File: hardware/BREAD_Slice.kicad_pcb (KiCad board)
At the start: 2 copper layers, 72.6 x 100 mm, 16 parts, among them J1 Conn_01x10_Female, J2 I2C_01x04

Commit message: Initial commit
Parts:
- removed C4: 22uF, Capacitor_SMD:C_1206_3216Metric
- removed D1: WS2812B_5050, SparkFun-LED:WS2812-5050-4PIN
- removed HS1: Heatsink_Pad, SparkFun-Fuse:Thermal Pad
- removed L1: 4.7uH, Inductor_SMD:L_1210_3225Metric
- added FB1: Ferrite_Bead_Small, OCI_UPL_FOOTPRINTS:R_1206_HandSoldering, B.Cu at (175.9, 81.4)
- added FB2: Ferrite_Bead_Small, OCI_UPL_FOOTPRINTS:R_1206_HandSoldering, B.Cu at (175.9, 76.3)
- added J3: Screw_Terminal_01x02, OCI_UPL_FOOTPRINTS:TerminalBlock_Pheonix_MKDS1.5-2pol, F.Cu at (184.8, 62.3)
- added J4: Screw_Terminal_01x02, OCI_UPL_FOOTPRINTS:TerminalBlock_Pheonix_MKDS1.5-2pol, F.Cu at (184.8, 100.4)
- added Q1: TIP120, Package_TO_SOT_THT:TO-220-3_Vertical, F.Cu at (144.2, 85.2)
- added Q2: TIP120, Package_TO_SOT_THT:TO-220-3_Vertical, F.Cu at (144.2, 72.5)
- added R1: 10k, OCI_UPL_FOOTPRINTS:R_1206_HandSoldering, B.Cu at (174.7, 100.4)
- added R2: 10k, OCI_UPL_FOOTPRINTS:R_1206_HandSoldering, B.Cu at (159.4, 91.5)
- added R3: 10k, OCI_UPL_FOOTPRINTS:R_1206_HandSoldering, B.Cu at (159.4, 83.9)
- C1: value 22uF -> 10uF_t; footprint Capacitor_SMD:C_1206_3216Metric -> OCI_UPL_FOOTPRINTS:C_2312
- C2: value 100nF -> 10uF_t; footprint Capacitor_SMD:C_1206_3216Metric -> OCI_UPL_FOOTPRINTS:C_2312
- C3: value 22uF -> 0.01 uF; footprint Capacitor_SMD:C_1206_3216Metric -> OCI_UPL_FOOTPRINTS:C_1206_HandSoldering
- H1, H4: footprint MountingHole:MountingHole_5mm -> MountingHole:MountingHole_3.2mm_M3_DIN965_Pad
- H2: renamed from H3; footprint MountingHole:MountingHole_5mm -> MountingHole:MountingHole_3.2mm_M3_DIN965_Pad
- H3: renamed from H2; footprint MountingHole:MountingHole_5mm -> MountingHole:MountingHole_3.2mm_M3_DIN965_Pad
- J2: value I2C_01x04 -> Screw_Terminal_01x02; footprint Connector_JST:JST_SH_SM04B-SRSS-TB_1x04-1MP_P1.00mm_Horizontal -> OCI_UPL_FOOTPRINTS:TerminalBlock_Pheonix_MKDS1.5-2pol; moved to F.Cu
- U1: value ~ -> MAX31855KASA; footprint Package_TO_SOT_SMD:TSOT-23-6 -> Package_SO:SOIC-8_3.9x4.9mm_P1.27mm
- moved Logo1 75.1 mm to (166.6, 135.8), turned to 0 degrees
- moved J2 69.4 mm to (184.8, 76.3), turned to -90 degrees
- moved C3 54.1 mm to (169.6, 78.8), turned to 90 degrees
- moved U1 53.6 mm to (159.4, 78.8), turned to 180 degrees
- moved C1 35.5 mm to (157.6, 99.0), turned to 0 degrees
- moved C2 32.3 mm to (157.6, 107.8), turned to 0 degrees
- moved A1 7.59 mm to (135.0, 100.0)
- moved J1 3.43 mm to (129.6, 78.8)
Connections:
- A1 pad 1: unconnected-(A1-D1/TX-Pad1) -> Net-(A1-Pad1)
- A1 pad 10: unconnected-(A1-D7-Pad10) -> Net-(A1-Pad10)
- A1 pad 11: unconnected-(A1-D8-Pad11) -> Net-(A1-Pad11)
- A1 pad 12: unconnected-(A1-D9-Pad12) -> /SS
- A1 pad 13: unconnected-(A1-D10-Pad13) -> /DATA
- A1 pad 14: unconnected-(A1-D11-Pad14) -> /CLK
- A1 pad 15: unconnected-(A1-D12-Pad15) -> Net-(A1-Pad15)
- A1 pad 16: unconnected-(A1-D13-Pad16) -> Net-(A1-Pad16)
- A1 pad 17: unconnected-(A1-3V3-Pad17) -> Net-(A1-Pad17)
- A1 pad 18: unconnected-(A1-AREF-Pad18) -> Net-(A1-Pad18)
- A1 pad 19: unconnected-(A1-A0-Pad19) -> /TMSTR
- A1 pad 2: unconnected-(A1-D0/RX-Pad2) -> Net-(A1-Pad2)
- A1 pad 20: unconnected-(A1-A1-Pad20) -> Net-(A1-Pad20)
- A1 pad 21: unconnected-(A1-A2-Pad21) -> Net-(A1-Pad21)
- A1 pad 22: unconnected-(A1-A3-Pad22) -> Net-(A1-Pad22)
- A1 pad 25: unconnected-(A1-A6-Pad25) -> Net-(A1-Pad25)
- A1 pad 26: unconnected-(A1-A7-Pad26) -> Net-(A1-Pad26)
- A1 pad 28: unconnected-(A1-~{RESET}-Pad28) -> Net-(A1-Pad28)
- A1 pad 3: unconnected-(A1-~{RESET}-Pad3) -> Net-(A1-Pad3)
- A1 pad 30: unconnected-(A1-VIN-Pad30) -> +12V
- A1 pad 8: /LED -> Net-(A1-Pad8)
- A1 pad 9: unconnected-(A1-D6-Pad9) -> /PWM
- C1 pad 1: GND -> +12V
- C1 pad 2: +12V -> GND
- C2 pad 1: Net-(U1-SW) -> +5V
- C2 pad 2: Net-(U1-BST) -> GND
- C3 pad 1: GND -> Net-(C3-Pad1)
- C3 pad 2: +5V -> Net-(C3-Pad2)
- J2 pad 1: GND -> Net-(FB2-Pad2)
- J2 pad 2: +5V -> Net-(FB1-Pad2)
- U1 pad 1: +5V -> GND
- U1 pad 2: +12V -> Net-(C3-Pad2)
- U1 pad 3: +12V -> Net-(C3-Pad1)
- U1 pad 4: GND -> +5V
- U1 pad 5: Net-(U1-SW) -> /CLK
- U1 pad 6: Net-(U1-BST) -> /SS
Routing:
- net /SS: track 0.00 -> 96.8 mm, vias 0 -> 2
- net GND: track 19.6 -> 91.1 mm, vias 14 -> 2
- net /DATA: track 0.00 -> 69.2 mm
- net /CLK: track 0.00 -> 68.8 mm
- net Net-(J3-Pad1): track 0.00 -> 65.2 mm
- net Net-(J3-Pad2): track 0.00 -> 63.8 mm
- net /E_STOP: track 30.1 -> 93.2 mm, vias 0 -> 2
- net +5V: track 108.9 -> 51.7 mm, vias 1 -> 0
- net /LED: track 51.5 -> 0.00 mm
- net /TMSTR: track 0.00 -> 46.6 mm
- net /PWM: track 0.00 -> 41.9 mm
- net /I2C_CLK: track 78.5 -> 42.6 mm
- net /I2C_DAT: track 76.6 -> 41.8 mm
- net +12V: track 46.8 -> 81.6 mm, vias 0 -> 2
- net Net-(C3-Pad2): track 0.00 -> 13.4 mm
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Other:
- board size 72.6 x 100 mm -> 70 x 100 mm
- board text added: "+"
- board text added: "-"
- board text added: "Heater"
- board text added: "Heating Slice SLC_HEAT R0 2021"
- board text added: "Thermistor Input"
- board text added: "Thermocouple Input"
- board text removed: "12V"
- board text removed: "12V->5V Reg"
- board text removed: "5V I2C Connector"
- board text removed: "ARDUINO NANO"
- board text removed: "BREAD Slice Template SLC_TEMP <version> <year>"
- board text removed: "ESTOP"
- board text removed: "GND"
- board text removed: "INT"
- board text removed: "LED"
- board text removed: "SCL"
- board text removed: "SDA"
- board text removed: "SYNC"

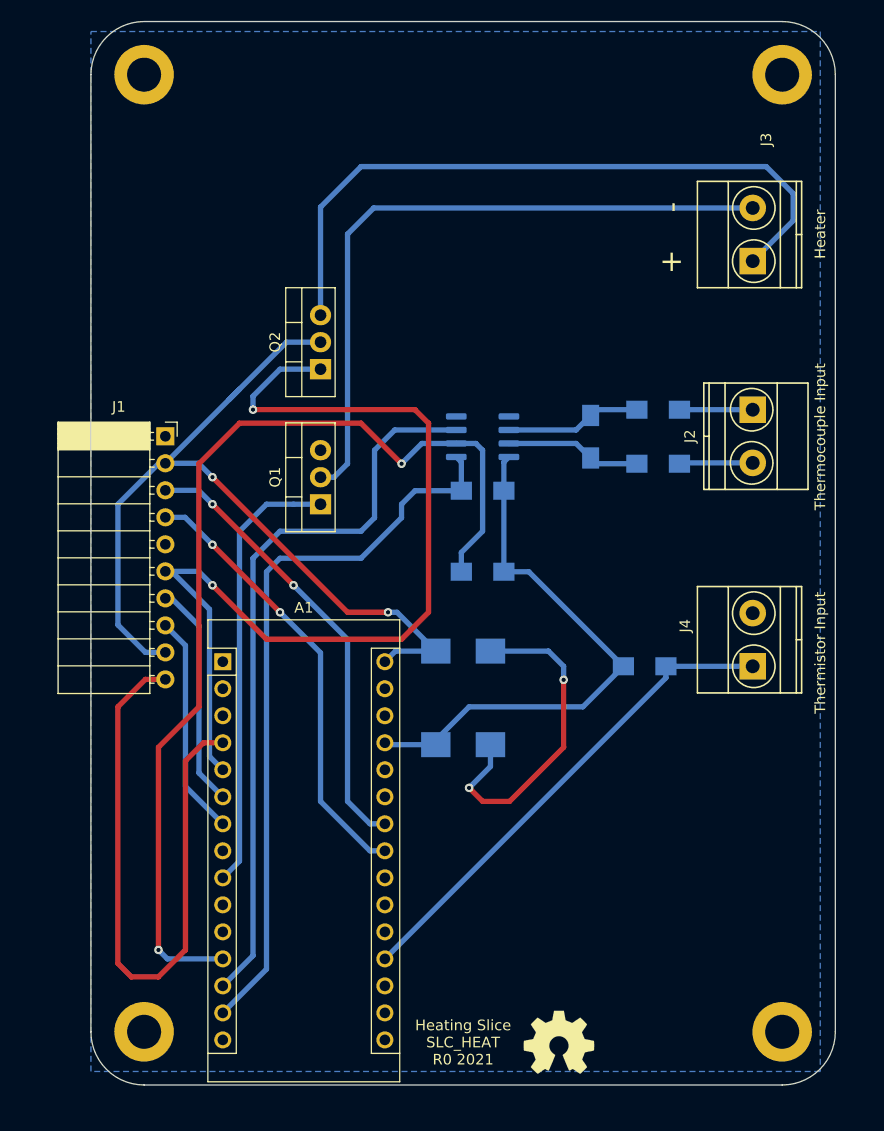
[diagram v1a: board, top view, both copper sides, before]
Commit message: upgraded by duplicating ciruit, new core, all back copper
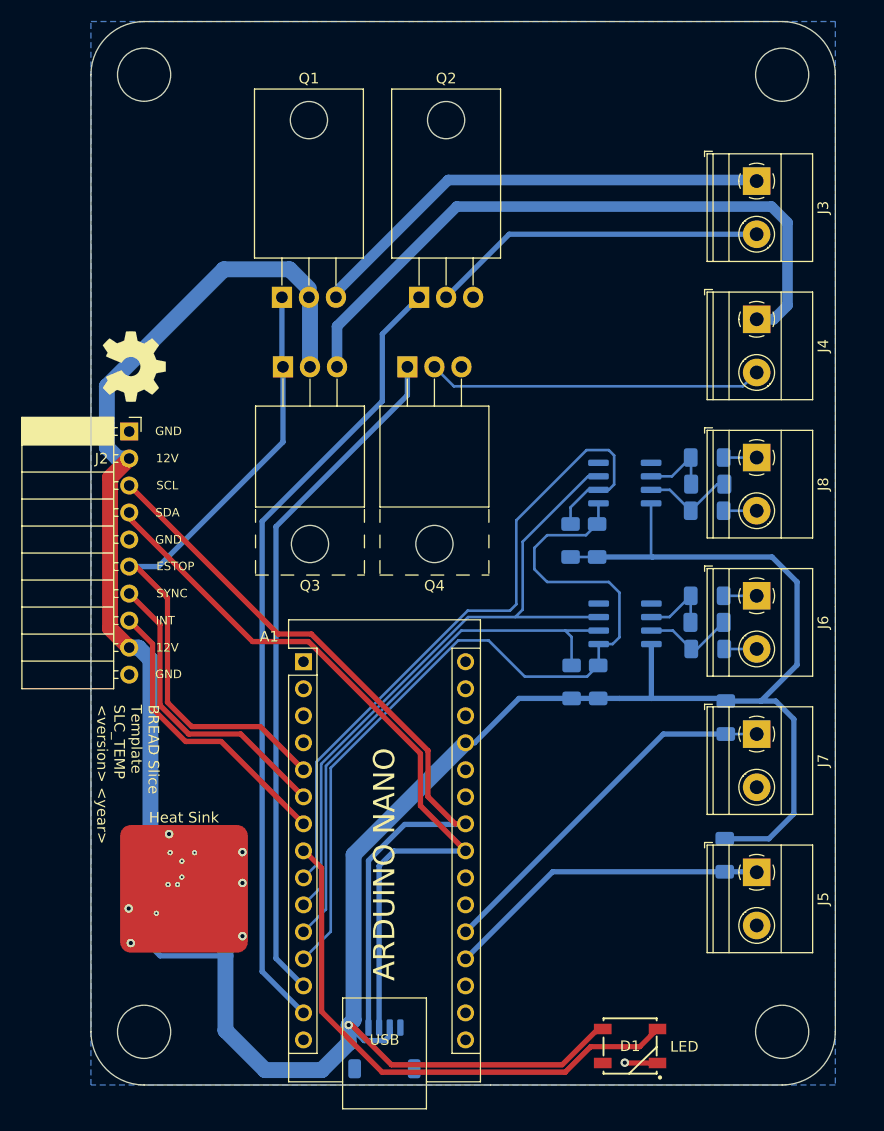
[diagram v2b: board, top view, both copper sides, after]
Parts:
- removed the J2 at (184.8, 76.3)
- added C4: 22uF, Capacitor_SMD:C_1206_3216Metric, B.Cu at (133.8, 116.5)
- added C5: 0.01 uF, Capacitor_SMD:C_1206_3216Metric_Pad1.33x1.80mm_HandSolder, B.Cu at (180.5, 96.3)
- added C6: 0.01 uF, Capacitor_SMD:C_1206_3216Metric_Pad1.33x1.80mm_HandSolder, B.Cu at (180.6, 83.3)
- added D1: WS2812B_5050, SparkFun-LED:WS2812-5050-4PIN, F.Cu at (173.3, 136.1)
- added FB3: Ferrite_Bead_Small, Resistor_SMD:R_1206_3216Metric_Pad1.30x1.75mm_HandSolder, B.Cu at (180.6, 85.8)
- added FB4: Ferrite_Bead_Small, Resistor_SMD:R_1206_3216Metric_Pad1.30x1.75mm_HandSolder, B.Cu at (180.6, 80.8)
- added HS1: Heatsink_Pad, KML-Custom:Thermal Pad, F.Cu at (131.3, 121.4)
- added J1: I2C_01x04, Connector_JST:JST_SH_SM04B-SRSS-TB_1x04-1MP_P1.00mm_Horizontal, B.Cu at (150.2, 136.4)
- added J5: Screw_Terminal_01x02, TerminalBlock_Phoenix:TerminalBlock_Phoenix_MKDS-1,5-2_1x02_P5.00mm_Horizontal, F.Cu at (185.2, 119.8)
- added J6: Screw_Terminal_01x02, TerminalBlock_Phoenix:TerminalBlock_Phoenix_MKDS-1,5-2_1x02_P5.00mm_Horizontal, F.Cu at (185.2, 93.8)
- added J7: Screw_Terminal_01x02, TerminalBlock_Phoenix:TerminalBlock_Phoenix_MKDS-1,5-2_1x02_P5.00mm_Horizontal, F.Cu at (185.2, 106.8)
- added J8: Screw_Terminal_01x02, TerminalBlock_Phoenix:TerminalBlock_Phoenix_MKDS-1,5-2_1x02_P5.00mm_Horizontal, F.Cu at (185.2, 80.8)
- added L1: 4.7uH, Inductor_SMD:L_1210_3225Metric, B.Cu at (133.8, 122.8)
- added Q3: TIP120, Package_TO_SOT_THT:TO-220-3_Horizontal_TabUp, F.Cu at (140.7, 72.3)
- added Q4: TIP120, Package_TO_SOT_THT:TO-220-3_Horizontal_TabUp, F.Cu at (152.4, 72.3)
- added R4: 10k, Resistor_SMD:R_1206_3216Metric_Pad1.30x1.75mm_HandSolder, B.Cu at (170.2, 88.6)
- added R5: 10k, Resistor_SMD:R_1206_3216Metric_Pad1.30x1.75mm_HandSolder, B.Cu at (167.7, 88.6)
- added R6: 10k, Resistor_SMD:R_1206_3216Metric_Pad1.30x1.75mm_HandSolder, B.Cu at (182.3, 105.2)
- added U2: MAX31855KASA, Package_SO:SOIC-8_3.9x4.9mm_P1.27mm, B.Cu at (172.8, 96.4)
- added U3: MAX31855KASA, Package_SO:SOIC-8_3.9x4.9mm_P1.27mm, B.Cu at (172.8, 83.2)
- C1: value 10uF_t -> 22uF; footprint OCI_UPL_FOOTPRINTS:C_2312 -> Capacitor_SMD:C_1206_3216Metric
- C2: value 10uF_t -> 100nF; footprint OCI_UPL_FOOTPRINTS:C_2312 -> Capacitor_SMD:C_1206_3216Metric
- C3: value 0.01 uF -> 22uF; footprint OCI_UPL_FOOTPRINTS:C_1206_HandSoldering -> Capacitor_SMD:C_1206_3216Metric
- FB1, FB2, R1, R2, R3: footprint OCI_UPL_FOOTPRINTS:R_1206_HandSoldering -> Resistor_SMD:R_1206_3216Metric_Pad1.30x1.75mm_HandSolder
- H1, H4: footprint MountingHole:MountingHole_3.2mm_M3_DIN965_Pad -> MountingHole:MountingHole_5mm
- H2: renamed from H3; footprint MountingHole:MountingHole_3.2mm_M3_DIN965_Pad -> MountingHole:MountingHole_5mm
- H3: renamed from H2; footprint MountingHole:MountingHole_3.2mm_M3_DIN965_Pad -> MountingHole:MountingHole_5mm
- J3, J4: footprint OCI_UPL_FOOTPRINTS:TerminalBlock_Pheonix_MKDS1.5-2pol -> TerminalBlock_Phoenix:TerminalBlock_Phoenix_MKDS-1,5-2_1x02_P5.00mm_Horizontal
- Q1, Q2: footprint Package_TO_SOT_THT:TO-220-3_Vertical -> Package_TO_SOT_THT:TO-220-3_Horizontal_TabDown
- U1: value MAX31855KASA -> ~; footprint Package_SO:SOIC-8_3.9x4.9mm_P1.27mm -> Package_TO_SOT_SMD:TSOT-23-6
- moved Logo1 75.1 mm to (126.7, 72.2), turned to -90 degrees
- moved C3 54.1 mm to (133.8, 119.5), turned to 0 degrees
- moved U1 53.6 mm to (128.8, 122.8), turned to 0 degrees
- moved R3 41.2 mm to (182.2, 118.2), turned to -90 degrees
- moved C1 35.5 mm to (128.6, 119.5), turned to 180 degrees
- moved J4 32.6 mm to (185.2, 67.8), turned to -90 degrees
- moved C2 32.3 mm to (131.2, 126.3), turned to 180 degrees
- moved Q1 19.8 mm to (140.6, 65.7), turned to 0 degrees
- moved FB2 18.1 mm to (180.6, 93.8)
- moved FB1 18.0 mm to (180.6, 98.8)
- moved R2 13.3 mm to (167.8, 101.9), turned to -90 degrees
- moved Q2 11.5 mm to (153.5, 65.7), turned to 0 degrees
- moved A1 7.59 mm to (142.6, 100.0)
- moved J3 7.54 mm to (185.2, 54.8), turned to -90 degrees
- moved R1 4.61 mm to (170.3, 101.9), turned to 90 degrees
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- renumbered J1 to J2
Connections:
- A1 pad 1: Net-(A1-Pad1) -> unconnected-(A1-D1/TX-Pad1)
- A1 pad 10: Net-(A1-Pad10) -> /DATA
- A1 pad 11: Net-(A1-Pad11) -> /SS1
- A1 pad 12: /SS -> /CLK
- A1 pad 13: /DATA -> /PWM2
- A1 pad 14: /CLK -> /PWM1
- A1 pad 15: Net-(A1-Pad15) -> unconnected-(A1-D12-Pad15)
- A1 pad 16: Net-(A1-Pad16) -> unconnected-(A1-D13-Pad16)
- A1 pad 17: Net-(A1-Pad17) -> unconnected-(A1-3V3-Pad17)
- A1 pad 18: Net-(A1-Pad18) -> unconnected-(A1-AREF-Pad18)
- A1 pad 19: /TMSTR -> /TMSTR1
- A1 pad 2: Net-(A1-Pad2) -> unconnected-(A1-D0/RX-Pad2)
- A1 pad 20: Net-(A1-Pad20) -> /TMSTR2
- A1 pad 21: Net-(A1-Pad21) -> unconnected-(A1-A2-Pad21)
- A1 pad 22: Net-(A1-Pad22) -> unconnected-(A1-A3-Pad22)
- A1 pad 25: Net-(A1-Pad25) -> unconnected-(A1-A6-Pad25)
- A1 pad 26: Net-(A1-Pad26) -> unconnected-(A1-A7-Pad26)
- A1 pad 28: Net-(A1-Pad28) -> unconnected-(A1-~{RESET}-Pad28)
- A1 pad 3: Net-(A1-Pad3) -> unconnected-(A1-~{RESET}-Pad3)
- A1 pad 30: +12V -> unconnected-(A1-VIN-Pad30)
- A1 pad 8: Net-(A1-Pad8) -> /LED
- A1 pad 9: /PWM -> /SS2
- C1 pad 1: +12V -> GND
- C1 pad 2: GND -> +12V
- C2 pad 1: +5V -> Net-(U1-SW)
- C2 pad 2: GND -> Net-(U1-BST)
- C3 pad 1: Net-(C3-Pad1) -> GND
- C3 pad 2: Net-(C3-Pad2) -> +5V
- FB1 pad 1: Net-(C3-Pad1) -> Net-(U2-T+)
- FB2 pad 1: Net-(C3-Pad2) -> Net-(U2-T-)
- J3 pad 1: Net-(J3-Pad1) -> Net-(J3-Pin_1)
- J3 pad 2: Net-(J3-Pad2) -> Net-(J3-Pin_2)
- J4 pad 1: /TMSTR -> Net-(J4-Pin_1)
- J4 pad 2: GND -> Net-(J4-Pin_2)
- Q1 pad 1: /PWM -> /E_STOP
- Q1 pad 2: Net-(J3-Pad2) -> +12V
- Q1 pad 3: GND -> Net-(J3-Pin_1)
- Q2 pad 1: /E_STOP -> /PWM1
- Q2 pad 2: +12V -> Net-(J3-Pin_2)
- Q2 pad 3: Net-(J3-Pad1) -> GND
- R1 pad 2: /TMSTR -> /CLK
- R2 pad 1: /SS -> /SS1
- R3 pad 2: /CLK -> /TMSTR1
- U1 pad 1: GND -> +5V
- U1 pad 2: Net-(C3-Pad2) -> +12V
- U1 pad 3: Net-(C3-Pad1) -> +12V
- U1 pad 4: +5V -> GND
- U1 pad 5: /CLK -> Net-(U1-SW)
- U1 pad 6: /SS -> Net-(U1-BST)
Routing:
- net +5V: track 51.7 -> 203.5 mm, vias 0 -> 1
- net /SS: track 96.8 -> 0.00 mm, vias 2 -> 0
- net /PWM1: track 0.00 -> 75.0 mm
- net GND: track 91.1 -> 19.6 mm, vias 2 -> 14
- net /SS2: track 0.00 -> 65.7 mm
- net Net-(J3-Pad1): track 65.2 -> 0.00 mm
- net /PWM2: track 0.00 -> 64.4 mm
- net Net-(J3-Pad2): track 63.8 -> 0.00 mm
- net Net-(J4-Pin_1): track 0.00 -> 62.8 mm
- net /LED: track 0.00 -> 51.5 mm
- net /SS1: track 0.00 -> 50.9 mm
- net /TMSTR: track 46.6 -> 0.00 mm
- net Net-(J3-Pin_1): track 0.00 -> 44.4 mm
- net /PWM: track 41.9 -> 0.00 mm
- net /TMSTR2: track 0.00 -> 35.1 mm
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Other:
- outline, holes or cut-outs redrawn
- board text added: "12V"
- board text added: "12V->5V Reg"
- board text added: "5V I2C Connector"
- board text added: "ARDUINO NANO"
- board text added: "BREAD Slice Template SLC_TEMP <version> <year>"
- board text added: "ESTOP"
- board text added: "GND"
- board text added: "INT"
- board text added: "LED"
- board text added: "SCL"
- board text added: "SDA"
- board text added: "SYNC"
- board text removed: "+"
- board text removed: "-"
- board text removed: "Heater"
- board text removed: "Heating Slice SLC_HEAT R0 2021"
- board text removed: "Thermistor Input"
- board text removed: "Thermocouple Input"
